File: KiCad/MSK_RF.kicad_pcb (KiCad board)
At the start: 2 copper layers, 69 parts, among them J1 Conn_ARM_JTAG_SWD_10, J2 Conn_01x12, J3 Conn_01x12, J4 Conn_Coaxial, J5 USB_B_Micro, SW1 SW_Push, SW2 SW_Push, SW3 SW_Push, U1 STM32WLE5CCU6, U2 ADG918BRM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

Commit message: pcb update
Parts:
- removed C28: 4.7nF, Capacitor_SMD:C_0603_1608Metric_Pad1.08x0.95mm_HandSolder
- removed D5: PESD5V0L4UW, Package_TO_SOT_SMD:SOT-665
- removed R2: 1M, Resistor_SMD:R_0603_1608Metric_Pad0.98x0.95mm_HandSolder
- removed SW1, SW2, SW3: SW_Push, SamacSys_Parts:FSM2J_1
- added D2: ESDALC6V1-1U2, SamacSys_Parts:ESDALC6V11U2, F.Cu at (142.5, 42.8)
- added J6: I2C_Sensor, Connector_PinHeader_2.54mm:PinHeader_1x04_P2.54mm_Vertical, F.Cu at (84.5, 89.6)
- added R11: 0, SamacSys_Parts:transition, F.Cu at (69.2, 110.2)
- added R12: 0, SamacSys_Parts:transition, F.Cu at (67.3, 130.1)
- added R13: 0, SamacSys_Parts:transition, F.Cu at (69.2, 130.0)
- added R14: 0, SamacSys_Parts:transition, F.Cu at (69.2, 135.2)
- added S1: Button FSM2JSMAATR, SamacSys_Parts:FSM2J_1, F.Cu at (57.0, 86.8)
- added S2: Button FSM2JSMAATR, SamacSys_Parts:FSM2J_1, F.Cu at (47.2, 86.7)
- added S3: Button FSM2JSMAATR, SamacSys_Parts:FSM2J_1, F.Cu at (52.5, 118.0)
- C17, C18, C19, C20, C21, C22, C23, C3, C31, C32, C4, C5, C6, C7, C8, C9, L1, R5, R6, R7: moved to B.Cu
- D1: footprint LED_SMD:LED_0603_1608Metric -> LED_SMD:LED_0603_1608Metric_Pad1.05x0.95mm_HandSolder
- D3, D4: value PESD5V0L4UW -> ESDALC6V1-1U2; footprint Package_TO_SOT_SMD:SOT-665 -> SamacSys_Parts:ESDALC6V11U2
- J1: value Conn_ARM_JTAG_SWD_10 -> SWD connector; footprint Connector_PinSocket_2.54mm:PinSocket_2x05_P2.54mm_Vertical -> Connector_PinHeader_2.54mm:PinHeader_1x04_P2.54mm_Vertical
- J5: value USB_B_Micro -> 47346-0001
- moved JP2 93.5 mm to (59.5, 133.8), turned to 180 degrees
- moved C25 88.5 mm to (48.2, 94.9), turned to -90 degrees
- moved L6 87.8 mm to (69.2, 124.9), turned to -90 degrees
- moved D1 86.4 mm to (54.2, 103.8)
- moved C32 85.2 mm to (58.6, 137.2)
- moved J2 83.7 mm to (84.5, 95.2)
- moved C11 82.7 mm to (66.5, 119.4), turned to -90 degrees
- moved J4 81.0 mm to (69.2, 144.0), turned to 90 degrees
- moved R7 80.6 mm to (62.2, 137.2)
- moved D3 79.5 mm to (51.3, 95.8), turned to -90 degrees
- moved C21 78.7 mm to (65.1, 97.8)
- moved JP3 78.2 mm to (55.5, 133.8), turned to 180 degrees
- moved L5 77.4 mm to (69.2, 117.9), turned to -90 degrees
- moved R8 76.8 mm to (60.7, 119.2), turned to 180 degrees
- moved C15 75.7 mm to (75.1, 118.8), turned to 180 degrees
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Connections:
- C13 pad 1: GND -> Net-(C13-Pad1)
- C13 pad 2: Net-(C13-Pad2) -> GND
- C25 pad 1: GND -> Net-(C25-Pad1)
- C25 pad 2: Net-(C25-Pad2) -> GND
- D3 pad 1: Net-(D3-Pad1) -> Net-(C25-Pad1)
- D3 pad 2: Net-(C13-Pad2) -> GND
- D4 pad 1: Net-(D4-Pad1) -> NRST
- D4 pad 2: Net-(C25-Pad2) -> GND
- J1 pad 2: PA13 -> PA14
- J1 pad 3: GND -> PA13
- J1 pad 4: PA14 -> GND
- J5 pad 6: Net-(C28-Pad1) -> (no net)
- R3 pad 2: Net-(D3-Pad1) -> Net-(C13-Pad1)
- R4 pad 2: Net-(D4-Pad1) -> Net-(C25-Pad1)
- U1 pad 23: Net-(C14-Pad2) -> Net-(R11-Pad1)
- U2 pad 4: Net-(C24-Pad2) -> Net-(R14-Pad1)
- U2 pad 5: Net-(C26-Pad2) -> Net-(R13-Pad1)
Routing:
- net 3.3V: track 0.00 -> 72.2 mm, vias 0 -> 6
- net Net-(C6-Pad1): track 0.00 -> 38.3 mm, vias 0 -> 3
- net Net-(C1-Pad1): track 0.00 -> 13.9 mm
- net PA15: track 0.00 -> 12.4 mm
- net Net-(C11-Pad1): track 0.00 -> 10.5 mm
- net Net-(JP1-Pad1): track 0.00 -> 9.90 mm
- net Net-(C29-Pad2): track 0.00 -> 9.88 mm
- net Net-(C2-Pad1): track 0.00 -> 8.11 mm
- net Net-(C9-Pad1): track 0.00 -> 8.08 mm, vias 0 -> 1
- net Net-(C11-Pad2): track 0.00 -> 7.70 mm
- net Net-(C10-Pad2): track 0.00 -> 7.29 mm
- net Net-(C14-Pad2): track 0.00 -> 7.22 mm
- net Net-(R7-Pad2): track 0.00 -> 6.52 mm, vias 0 -> 1
- net Net-(U1-Pad27): track 0.00 -> 6.46 mm
- net Net-(C24-Pad1): track 0.00 -> 5.28 mm
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
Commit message: almost finished pcb
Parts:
- removed J1: SWD connector, Connector_PinHeader_2.54mm:PinHeader_1x04_P2.54mm_Vertical
- removed J6: I2C_Sensor, Connector_PinHeader_2.54mm:PinHeader_1x04_P2.54mm_Vertical
- removed JP2: Jumper_2_Bridged, Connector_PinHeader_2.54mm:PinHeader_1x02_P2.54mm_Vertical
- removed JP3: Jumper_2_Open, Connector_PinHeader_2.54mm:PinHeader_1x02_P2.54mm_Vertical
- removed R11, R12, R13, R14: 0, SamacSys_Parts:transition
- C9: moved to F.Cu
- moved D2 101.9 mm to (56.5, 97.5), turned to 180 degrees
- moved C27 97.3 mm to (56.9, 117.8)
- moved R3 97.0 mm to (55.6, 100.8)
- moved D4 96.7 mm to (57.7, 115.8), turned to 180 degrees
- moved C13 88.1 mm to (55.6, 99.0), turned to 180 degrees
- moved C32 21.8 mm to (78.9, 129.3), turned to 180 degrees
- moved C18 16.7 mm to (57.5, 109.6), turned to 90 degrees
- moved C29 15.6 mm to (77.1, 92.3), turned to 90 degrees
- moved R7 15.5 mm to (75.4, 129.3), turned to 180 degrees
- moved R10 12.8 mm to (75.1, 92.4), turned to -90 degrees
- moved J5 11.6 mm to (71.4, 82.3)
- moved D7 10.8 mm to (71.9, 93.3), turned to 0 degrees
- moved S3 8.13 mm to (53.2, 126.0)
- moved C1 7.97 mm to (77.5, 96.5)
- moved U3 7.85 mm to (71.6, 90.5), turned to 180 degrees
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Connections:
- C14 pad 2: Net-(C14-Pad2) -> Net-(U1-Pad23)
- C24 pad 2: Net-(C24-Pad2) -> Net-(U2-Pad4)
- C32 pad 2: Net-(C32-Pad2) -> FE_CTRL
- J3 pad 4: GND -> 3.3V
- J3 pad 5: GND -> PB12
- L4 pad 2: Net-(C14-Pad2) -> Net-(U1-Pad23)
- L5 pad 1: Net-(C14-Pad2) -> Net-(U1-Pad23)
- R7 pad 1: Net-(C32-Pad2) -> FE_CTRL
- U1 pad 23: Net-(R11-Pad1) -> Net-(U1-Pad23)
- U1 pad 32: GND -> PB12
- U2 pad 4: Net-(R14-Pad1) -> Net-(U2-Pad4)
- U2 pad 5: Net-(R13-Pad1) -> Net-(C26-Pad2)
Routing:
- net 3.3V: track 72.2 -> 209.5 mm, vias 6 -> 7
- net NRST: track 0.00 -> 53.7 mm, vias 0 -> 1
- net PA11: track 0.00 -> 44.8 mm, vias 0 -> 1
- net PA1: track 0.00 -> 43.4 mm
- net PA8: track 0.00 -> 41.6 mm, vias 0 -> 1
- net PB6: track 0.00 -> 41.0 mm, vias 0 -> 1
- net PB7: track 0.00 -> 38.5 mm, vias 0 -> 1
- net PA9: track 0.00 -> 35.8 mm, vias 0 -> 1
- net PA0: track 0.00 -> 35.5 mm
- net PA7: track 0.00 -> 30.5 mm
- net PA5: track 0.00 -> 28.1 mm
- net PA4: track 0.00 -> 26.6 mm
- net PA3: track 0.00 -> 26.0 mm
- net PA2: track 0.00 -> 25.1 mm
- net PA14: track 0.00 -> 22.8 mm, vias 0 -> 1
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- added copper zone on F.Cu, net GND
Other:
- board outline added: 48.8 x 63 mm

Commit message: pcb update
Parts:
- added J1: Conn_01x05_Male, Connector_PinHeader_2.54mm:PinHeader_1x05_P2.54mm_Vertical, F.Cu at (84.5, 77.5)
- moved J5 9.59 mm to (70.5, 72.8)
- moved C29 9.52 mm to (76.2, 82.9)
- moved R10 9.52 mm to (74.2, 82.9)
- moved S2 9.15 mm to (46.8, 82.7)
- moved C30 7.63 mm to (67.3, 84.8)
- moved U3 7.63 mm to (70.7, 83.0)
- moved S1 7.55 mm to (59.2, 82.8)
- moved D7 7.11 mm to (74.2, 86.6), turned to 90 degrees
- moved R8 2.59 mm to (59.5, 127.4)
- moved JP1 2.54 mm to (59.5, 121.2)
- moved S3 1.75 mm to (51.5, 126.0)
- moved C1 0.25 mm to (77.5, 96.2)
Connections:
- J3 pad 5: PB12 -> GND
- U1 pad 32: PB12 -> GND
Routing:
- net GND: track 0.00 -> 43.9 mm, vias 0 -> 230
- net NRST: track 53.7 -> 78.3 mm
- net 3.3V: track 209.5 -> 231.6 mm
- net PA13: track 16.7 -> 35.7 mm
- net Net-(C25-Pad1): track 7.17 -> 23.7 mm
- net Net-(C13-Pad1): track 6.90 -> 22.7 mm
- net PA14: track 22.8 -> 36.3 mm
- net Net-(C29-Pad2): track 9.49 -> 11.4 mm
- net Net-(JP1-Pad1): track 13.7 -> 15.2 mm
- net (no net): vias 0 -> 1
- added copper zone on B.Cu, net GND
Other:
- board size 48.8 x 63 mm -> 53.2 x 73.2 mm

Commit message: finished pcb
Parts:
- moved Y2 3.04 mm to (78.2, 109.0)
- moved C8 3.02 mm to (77.1, 104.0)
- moved Y1 2.76 mm to (73.0, 96.0)
- moved C2 2.26 mm to (77.8, 98.0)
- moved C1 2.06 mm to (78.0, 94.2)
- moved C22 1.03 mm to (73.0, 98.6)
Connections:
- J3 pad 1: unconnected-(J3-Pad1) -> 3.3V
- J3 pad 4: 3.3V -> PB12
- J3 pad 5: GND -> PA6
- U1 pad 14: GND -> PA6
- U1 pad 32: GND -> PB12
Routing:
- net PB12: track 0.00 -> 45.6 mm, vias 0 -> 1
- net PA6: track 0.00 -> 44.5 mm
- net 3.3V: track 231.6 -> 242.6 mm
- net Net-(C6-Pad1): track 39.5 -> 45.9 mm
- net Net-(U1-Pad26): track 4.30 -> 7.59 mm
- net Net-(C1-Pad1): track 11.3 -> 14.0 mm
- net Net-(U1-Pad27): track 6.46 -> 9.12 mm
- net Net-(C2-Pad1): track 8.83 -> 11.2 mm
- net PA14: track 36.3 -> 35.5 mm
- net GND: vias 230 -> 240
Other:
- board size 53.2 x 73.2 mm -> 49.2 x 73.2 mm

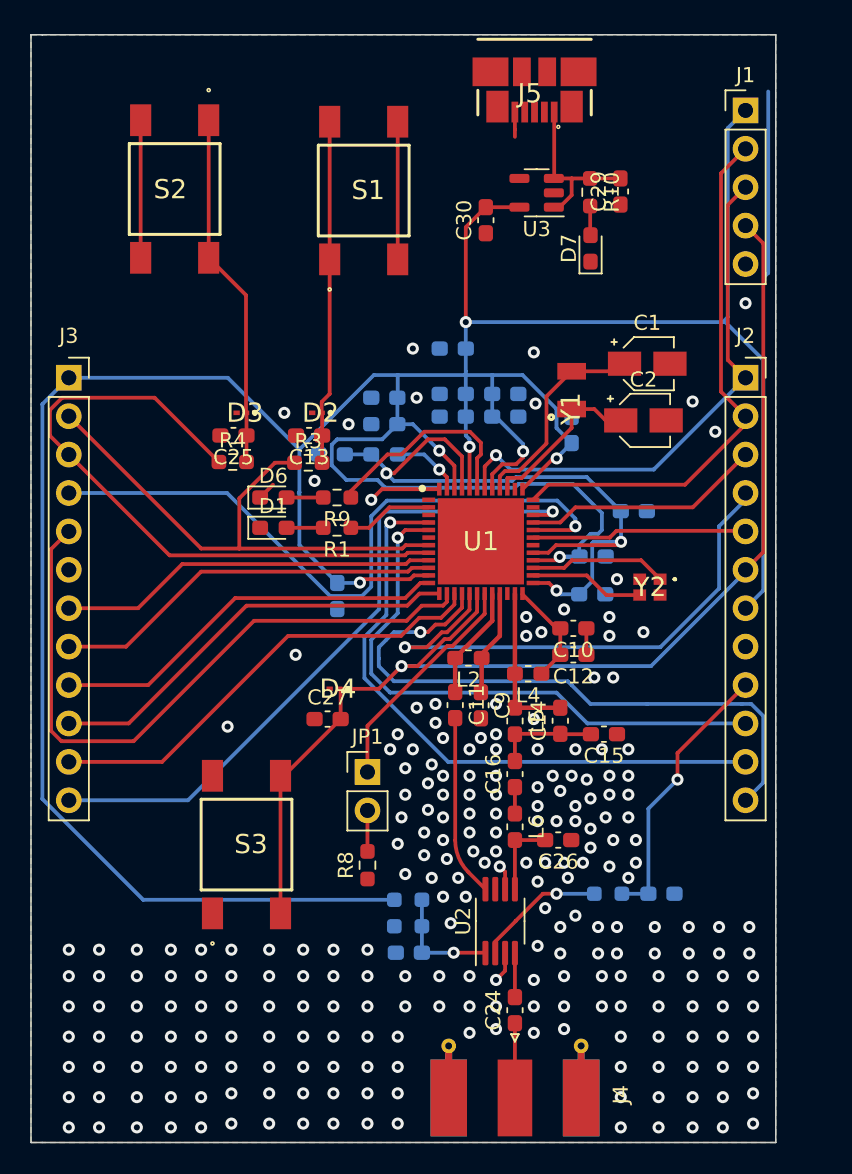
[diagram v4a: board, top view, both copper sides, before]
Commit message: added pin description
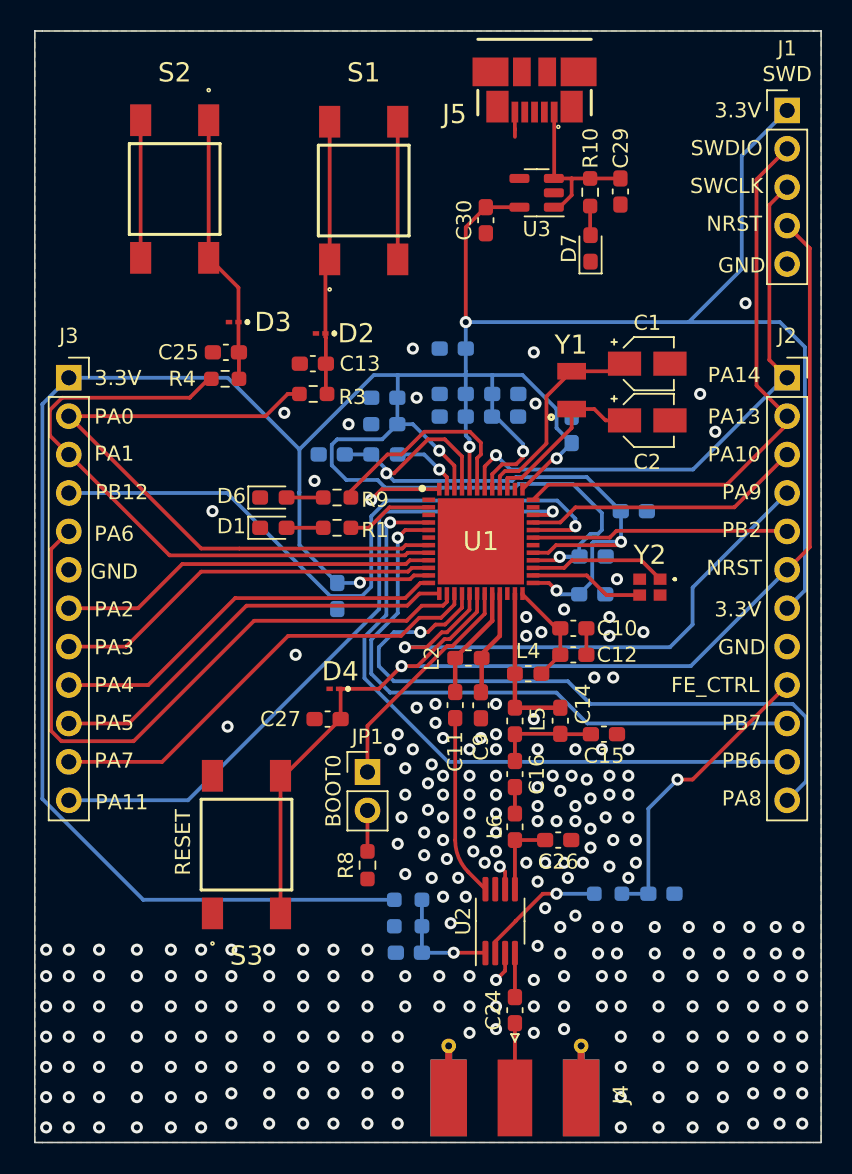
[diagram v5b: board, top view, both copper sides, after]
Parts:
- moved D3 6.02 mm to (51.0, 91.5)
- moved C25 5.52 mm to (50.1, 93.5)
- moved R4 5.52 mm to (50.1, 95.2)
- moved D2 5.26 mm to (56.8, 92.2)
- moved C13 4.76 mm to (55.9, 94.2)
- moved R3 4.56 mm to (55.9, 96.2)
- moved J1 2.75 mm to (87.2, 77.5)
- moved J2 2.75 mm to (87.2, 95.2)
- moved C2 0.25 mm to (78.0, 98.0)
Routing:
- net GND: track 43.9 -> 30.1 mm, vias 240 -> 264
- net PA0: track 35.5 -> 43.4 mm
- net Net-(C25-Pad1): track 23.7 -> 17.9 mm
- net 3.3V: track 242.6 -> 247.9 mm
- net Net-(C13-Pad1): track 22.7 -> 18.2 mm
- net PA13: track 35.7 -> 38.8 mm
- net NRST: track 78.3 -> 81.3 mm
- net PA8: track 41.6 -> 44.4 mm
- net PB6: track 41.0 -> 43.8 mm
- net PB2: track 14.3 -> 17.0 mm
- net PA14: track 35.5 -> 38.3 mm
- net PA10: track 15.9 -> 18.7 mm
- net PB7: track 38.5 -> 40.8 mm
- net PA1: track 43.4 -> 41.6 mm
- net FE_CTRL: track 18.2 -> 19.9 mm
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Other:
- board size 49.2 x 73.2 mm -> 52 x 73.5 mm
- board text added: "3.3V"
- board text added: "BOOT0"
- board text added: "FE_CTRL"
- board text added: "GND"
- board text added: "NRST"
- board text added: "PA0"
- board text added: "PA1"
- board text added: "PA10"
- board text added: "PA11"
- board text added: "PA13"
- board text added: "PA14"
- board text added: "PA2"
- board text added: "PA3"
- board text added: "PA4"
- board text added: "PA5"
- board text added: "PA6"
- board text added: "PA7"
- board text added: "PA8"
- board text added: "PA9"
- board text added: "PB12"
- board text added: "PB2"
- board text added: "PB6"
- board text added: "PB7"
- board text added: "RESET"
- board text added: "SWCLK"
- board text added: "SWD"
- board text added: "SWDIO"
